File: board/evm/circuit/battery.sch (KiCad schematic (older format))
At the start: 68 parts

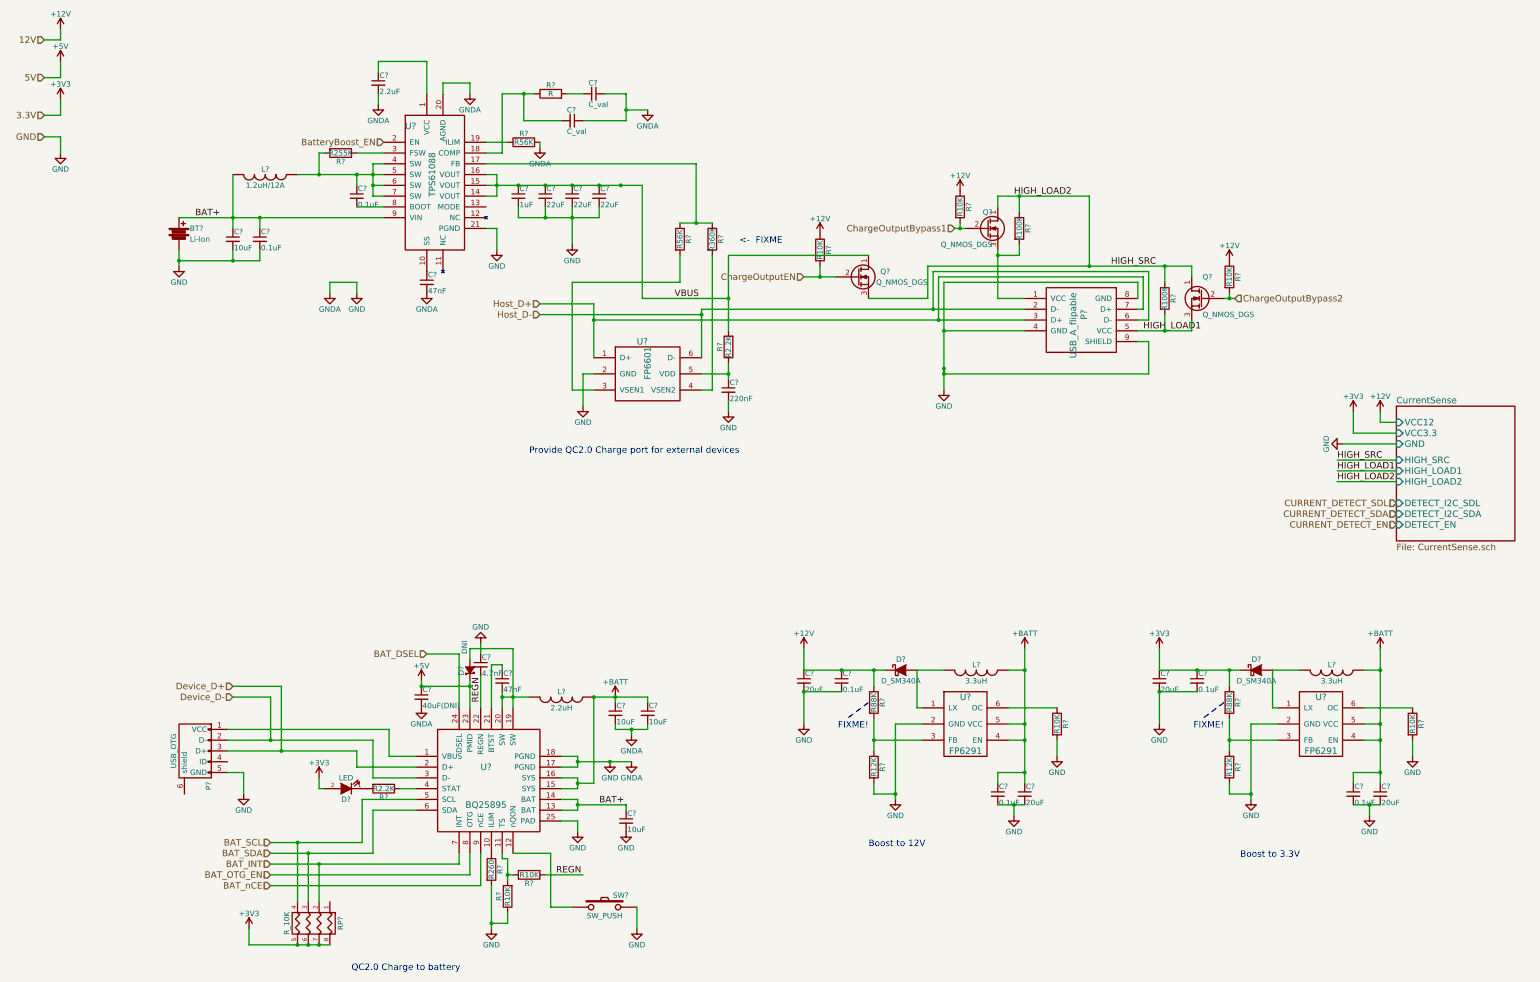
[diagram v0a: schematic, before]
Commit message: minor updates
- add lots of test points
- export usart1
- bug fix
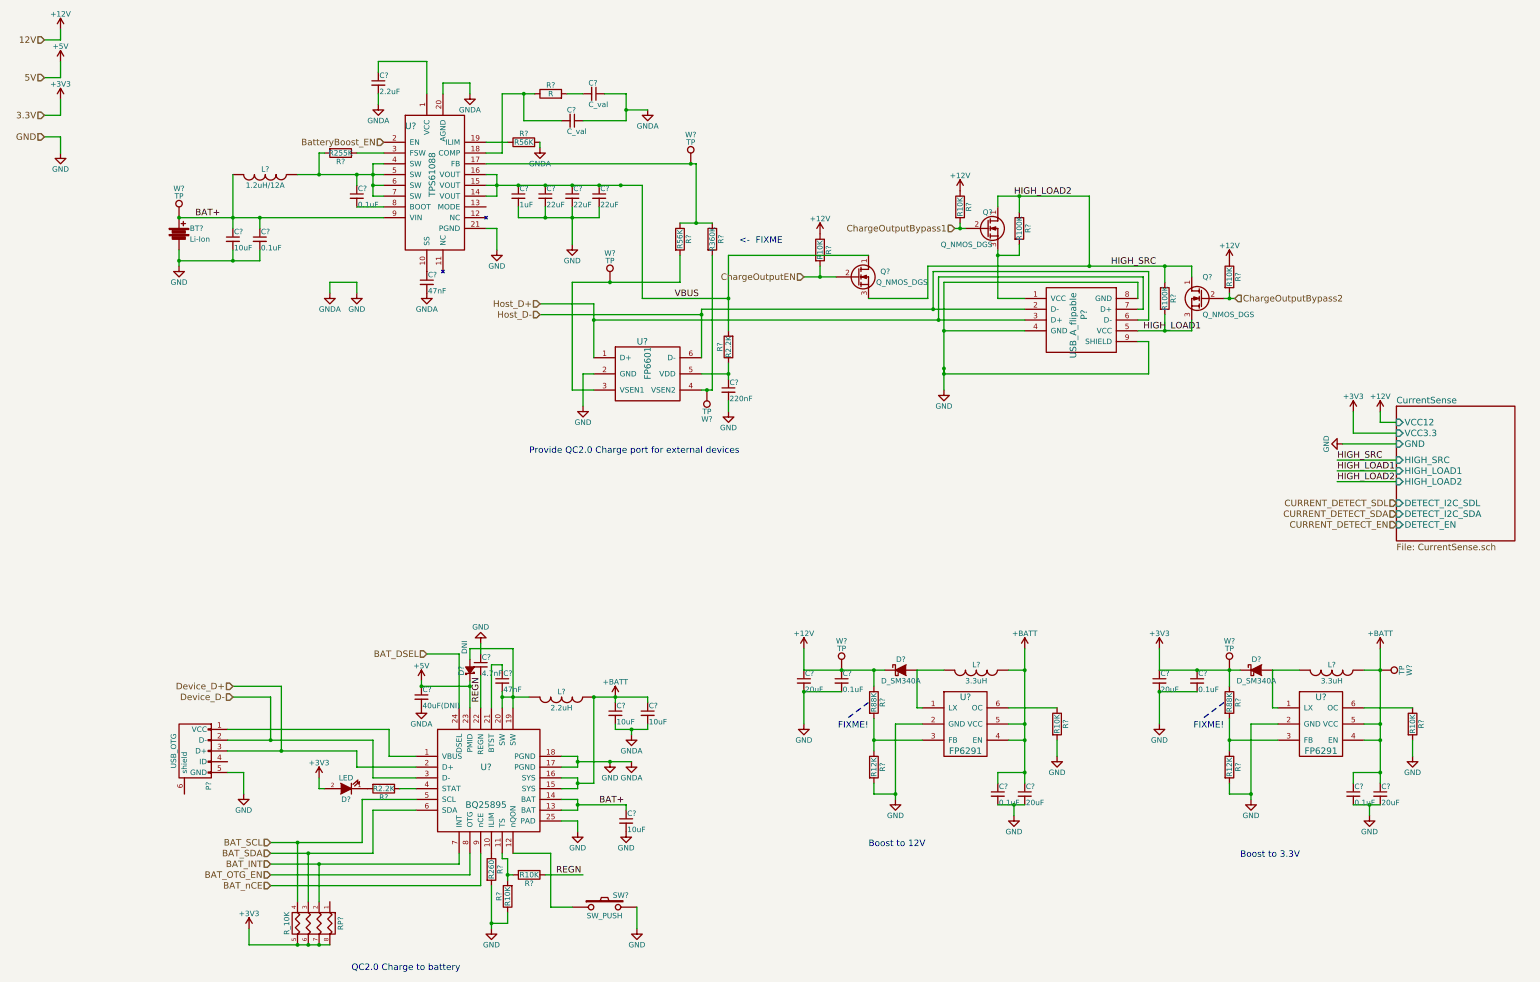
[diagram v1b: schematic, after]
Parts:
- added W? (x7): TP, symbol TEST_1P
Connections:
- net +12V: now also W?.1
- net +3V3: now also W?.1
- net +BATT: now also W?.1
- net BAT+: now also W?.1
- net at R?.1, R?.1, U?.17 (FB): now also W?.1
- net at R?.2, U?.4 (VSEN2): now also W?.1
- net at R?.2, U?.3 (VSEN1): now also W?.1
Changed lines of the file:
@@
 Text HLabel 14000 5200 0    60   Input ~ 0
 CURRENT_DETECT_SDL
+$Comp
+L TEST_1P W?
+U 1 1 57642F75
+P 7450 2050
+F 0 "W?" H 7450 2320 50  0000 C CNN
+F 1 "TP" H 7450 2250 50  0000 C CNN
+F 2 "" H 7650 2050 50  0000 C CNN
+F 3 "" H 7650 2050 50  0000 C CNN
+	1    7450 2050
+	1    0    0    -1
+$EndComp
+Connection ~ 7450 2050
+$Comp
+L TEST_1P W?
+U 1 1 576431FA
+P 6700 3150
+F 0 "W?" H 6700 3420 50  0000 C CNN
+F 1 "TP" H 6700 3350 50  0000 C CNN
+F 2 "" H 6900 3150 50  0000 C CNN
+F 3 "" H 6900 3150 50  0000 C CNN
+	1    6700 3150
+	1    0    0    -1
+$EndComp
+$Comp
+L TEST_1P W?
+U 1 1 57643914
+P 7600 4150
+F 0 "W?" H 7600 4420 50  0000 C CNN
+F 1 "TP" H 7600 4350 50  0000 C CNN
+F 2 "" H 7800 4150 50  0000 C CNN
+F 3 "" H 7800 4150 50  0000 C CNN
+	1    7600 4150
+	-1   0    0    1
+$EndComp
+Connection ~ 7600 4150
+Connection ~ 6700 3150
+$Comp
+L TEST_1P W?
+U 1 1 57647583
+P 13850 6750
+F 0 "W?" H 13850 7020 50  0000 C CNN
+F 1 "TP" H 13850 6950 50  0000 C CNN
+F 2 "" H 14050 6750 50  0000 C CNN
+F 3 "" H 14050 6750 50  0000 C CNN
+	1    13850 6750
+	0    1    1    0
+$EndComp
+$Comp
+L TEST_1P W?
+U 1 1 5764814E
+P 8850 6750
+F 0 "W?" H 8850 7020 50  0000 C CNN
+F 1 "TP" H 8850 6950 50  0000 C CNN
+F 2 "" H 9050 6750 50  0000 C CNN
+F 3 "" H 9050 6750 50  0000 C CNN
+	1    8850 6750
+	1    0    0    -1
+$EndComp
+$Comp
+L TEST_1P W?
+U 1 1 5764877D
+P 12450 6750
+F 0 "W?" H 12450 7020 50  0000 C CNN
+F 1 "TP" H 12450 6950 50  0000 C CNN
+F 2 "" H 12650 6750 50  0000 C CNN
+F 3 "" H 12650 6750 50  0000 C CNN
+	1    12450 6750
+	1    0    0    -1
+$EndComp
+$Comp
+L TEST_1P W?
+U 1 1 5764C228
+P 2700 2550
+F 0 "W?" H 2700 2820 50  0000 C CNN
+F 1 "TP" H 2700 2750 50  0000 C CNN
+F 2 "" H 2900 2550 50  0000 C CNN
+F 3 "" H 2900 2550 50  0000 C CNN
+	1    2700 2550
+	1    0    0    -1
+$EndComp
+Connection ~ 2700 2550
 $EndSCHEMATC

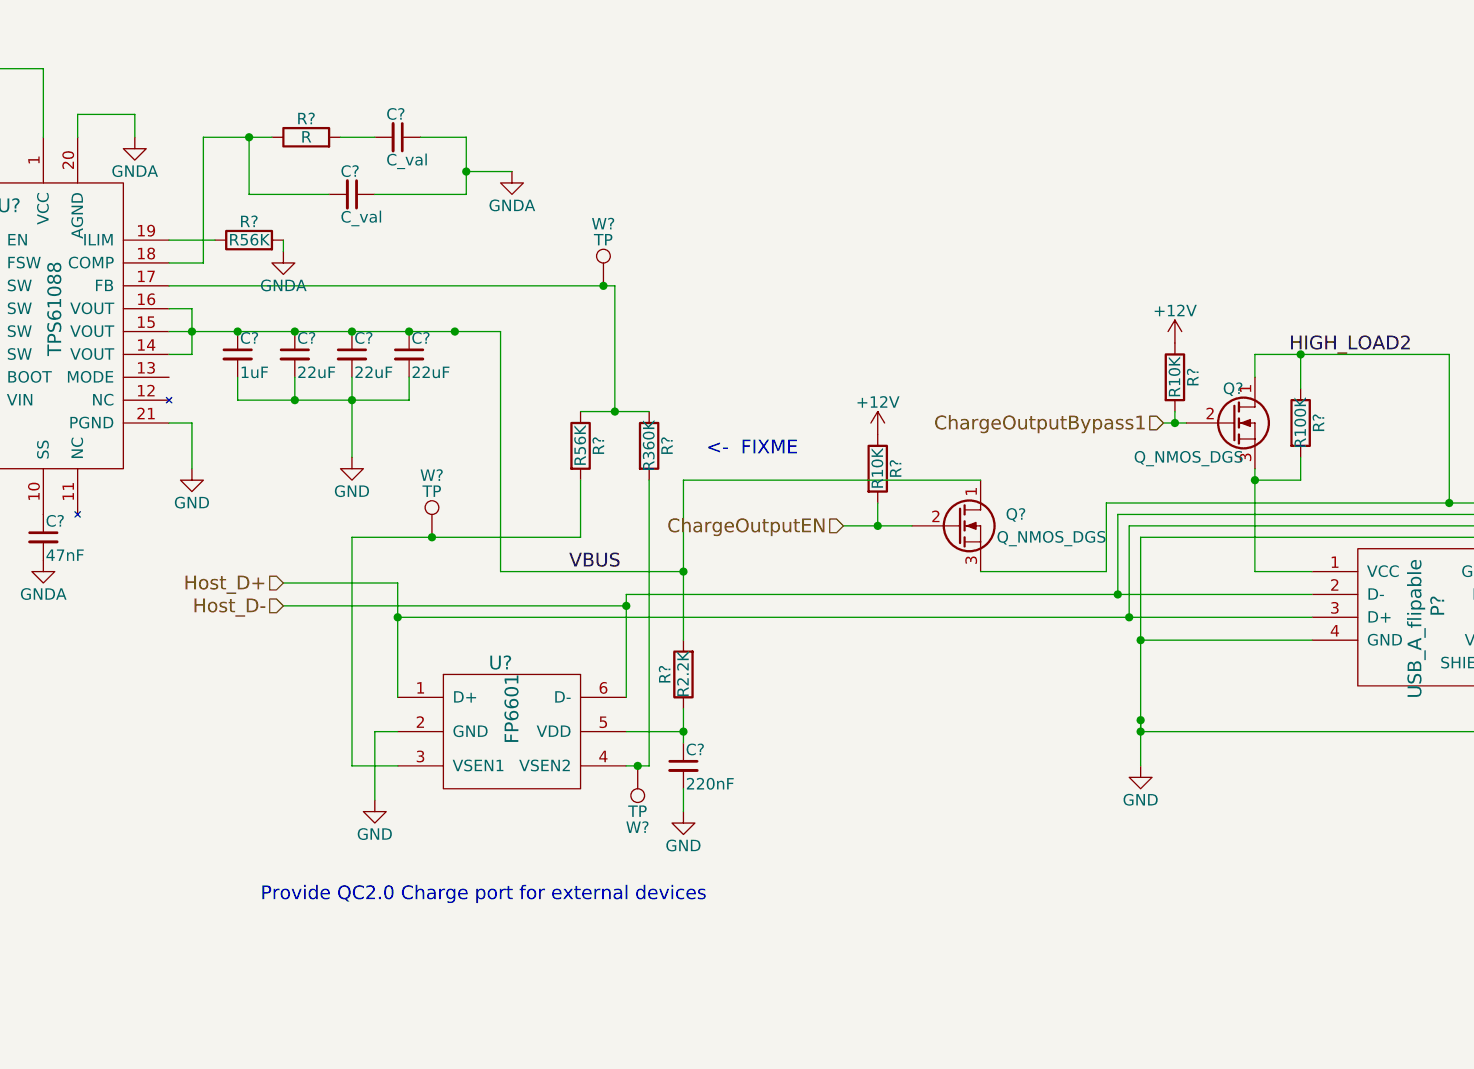
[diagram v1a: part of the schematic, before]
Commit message: upgrade qc2.0 output to qc3.0
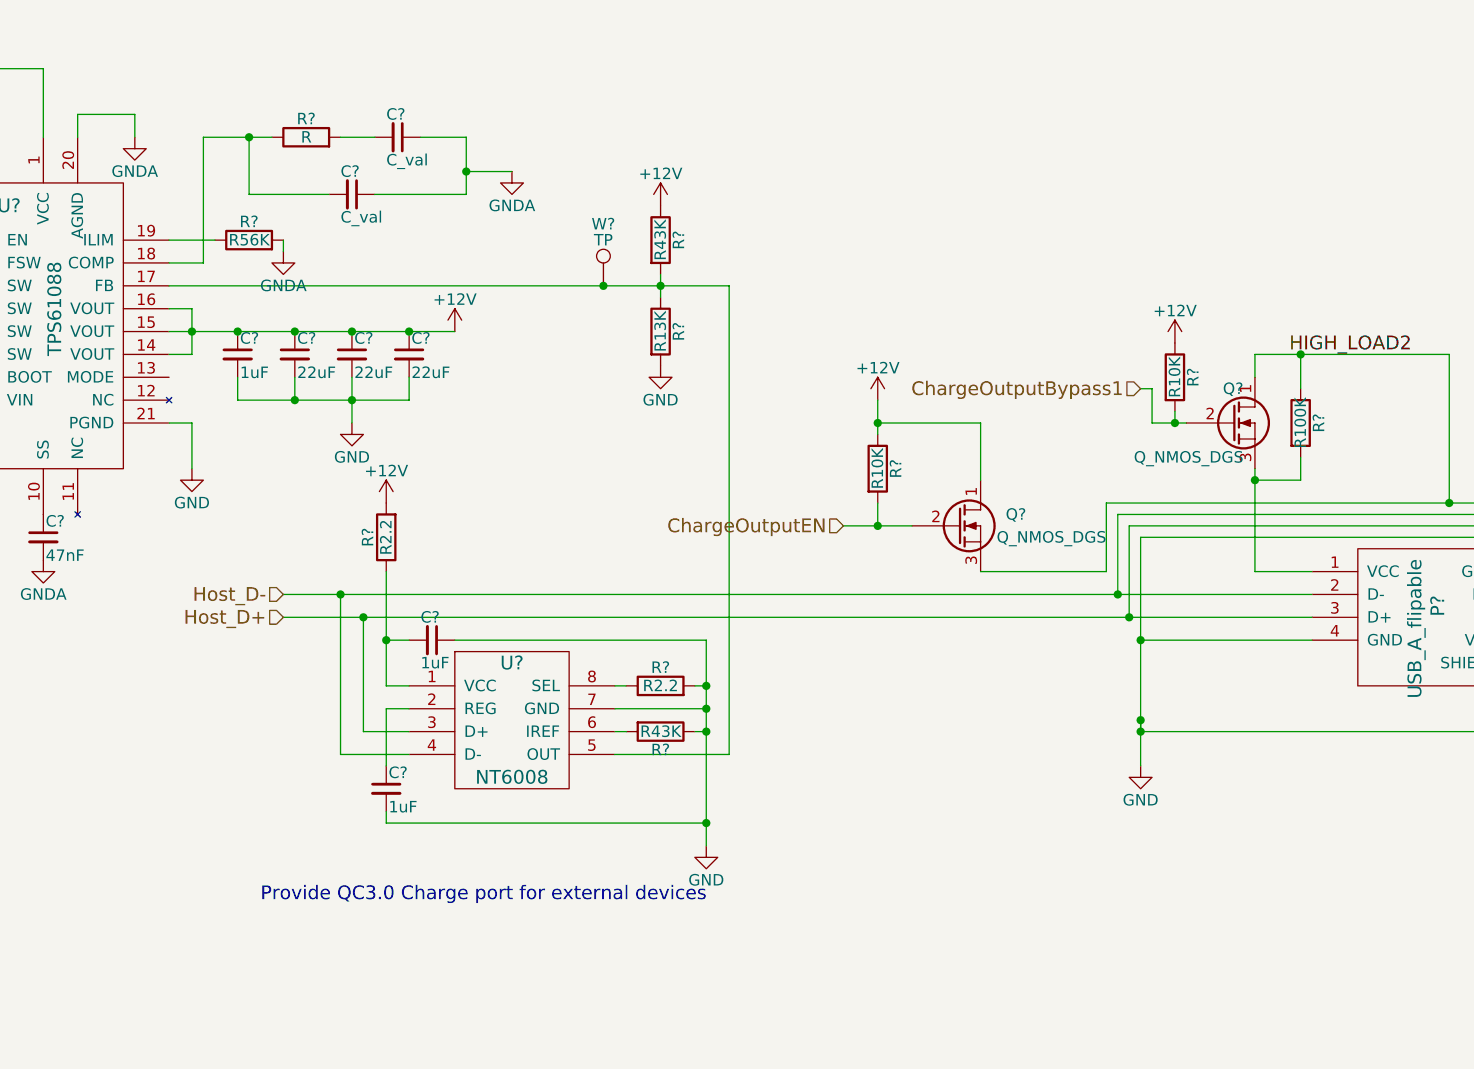
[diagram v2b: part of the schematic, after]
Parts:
- removed C?: 220nF, symbol C_Small
- removed R?: R360K, symbol R
- removed R?: R56K, symbol R
- removed U?: FP6601, symbol FP6601
- removed W? (x2): TP, symbol TEST_1P
- added C? (x2): 1uF, symbol C_Small
- added R?: R2.2, symbol R
- added R? (x2): R43K, symbol R
- added R?: R13K, symbol R
- added U?: NT6008, symbol NT6008
- R?: value R2.2K -> R2.2
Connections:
- net VBUS is gone; now on net +12V: C?.1, C?.1, C?.1, C?.1, Q?.1 (D), R?.2, U?.14 (VOUT), U?.15 (VOUT), U?.16 (VOUT)
- net +12V: now also R?.1
- net GND: now also C?.1, C?.2, R?.1, R?.2, R?.2, U?.7 (GND)
- net Host_D+: now also U?.3 (D+)
- net Host_D-: now also U?.4 (D-)
- net at U?.17 (FB), W?.1: now also R?.1, R?.2, U?.5 (OUT)
- net at R?.1: now also C?.2, U?.1 (VCC)
- new net: C?.1, U?.2 (REG)
- new net: R?.2, U?.6 (IREF)
- new net: R?.1, U?.8 (SEL)
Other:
- note added: "Provide QC3.0 Charge port for external devices"
- note removed: "<- FIXME"
- note removed: "Provide QC2.0 Charge port for external devices"
- moved on the sheet: R?

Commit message: working on drc
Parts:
- gave numbers to parts that had none: 76

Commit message: working on footprint
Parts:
- BT1: footprint (none) -> Connect:PINHEAD1-2
- C38, C42, C47, C49, C52, C54, C55, C56, C57, C60, C61, C64: footprint (none) -> Capacitors_SMD:C_0805
- C39, C40, C43, C44, C45, C48, C51, C58, C59, C62, C63: footprint (none) -> Capacitors_SMD:C_0402
- C41, C46, C50, C53: footprint (none) -> Capacitors_SMD:C_0603
- D11: footprint (none) -> LEDs:LED_0805
- D12: value DNI -> SS14(DNI); footprint (none) -> Diodes_SMD:SMA_Standard
- D13, D14: value D_SM340A -> D_SS14; footprint (none) -> Diodes_SMD:SMA_Standard
- R16, R17, R18, R19, R20, R21, R22, R23, R24, R25, R26, R27, R28, R29, R30, R31, R32, R33, R34, R35, R36, R37, R38, RP8: footprint (none) -> Resistors_SMD:R_0402
- SW9: footprint (none) -> Buttons_Switches_SMD:SW_SPST_B3U-1000P
- W49, W50, W51, W52, W53: footprint (none) -> Connect:PINTST

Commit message: still working on footprint
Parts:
- U12: footprint (none) -> My custom footprint:S-PVQFN-N20
- U14: footprint (none) -> My custom footprint:TSOT23-8L
- U15, U16: footprint (none) -> TO_SOT_Packages_SMD:SOT-23-6
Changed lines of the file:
@@
 LIBS:contrib
 LIBS:valves
+LIBS:stm8
+LIBS:stm32
+LIBS:74xgxx
+LIBS:ac-dc
+LIBS:actel
 LIBS:Altera
+LIBS:analog_devices
+LIBS:battery_management
+LIBS:bbd
+LIBS:brooktre
+LIBS:cmos_ieee
+LIBS:dc-dc
+LIBS:diode
+LIBS:elec-unifil
+LIBS:ESD_Protection
+LIBS:ftdi
+LIBS:gennum
+LIBS:graphic
+LIBS:hc11
+LIBS:ir
+LIBS:Lattice
+LIBS:logo
+LIBS:maxim
+LIBS:microchip_dspic33dsc
+LIBS:microchip_pic10mcu
+LIBS:microchip_pic12mcu
+LIBS:microchip_pic16mcu
+LIBS:microchip_pic18mcu
+LIBS:microchip_pic32mcu
+LIBS:motor_drivers
+LIBS:msp430
+LIBS:nordicsemi
+LIBS:nxp_armmcu
+LIBS:onsemi
+LIBS:Oscillators
+LIBS:powerint
+LIBS:Power_Management
+LIBS:pspice
+LIBS:references
+LIBS:relays
+LIBS:rfcom
+LIBS:sensors
+LIBS:silabs
+LIBS:supertex
+LIBS:switches
+LIBS:transf
+LIBS:ttl_ieee
+LIBS:video
+LIBS:Worldsemi
+LIBS:Xicor
+LIBS:Zilog
 LIBS:my_kicad
-LIBS:Oscillators
 LIBS:oh-my-keyboard-cache
 EELAYER 25 0
@@
 F 0 "U12" H 4850 2800 60  0000 C CNN
 F 1 "TPS61088" V 5050 2350 60  0000 C CNN
-F 2 "" H 5200 2250 60  0001 C CNN
+F 2 "My custom footprint:S-PVQFN-N20" H 5200 2250 60  0001 C CNN
 F 3 "" H 5200 2250 60  0000 C CNN
 	1    5200 2250
@@
 F 0 "U15" H 10000 7500 60  0000 C CNN
 F 1 "FP6291" H 10000 7000 60  0000 C CNN
-F 2 "" H 9950 7200 60  0001 C CNN
+F 2 "TO_SOT_Packages_SMD:SOT-23-6" H 9950 7200 60  0001 C CNN
 F 3 "" H 9950 7200 60  0000 C CNN
 	1    10000 7250
@@
 F 0 "U16" H 13300 7500 60  0000 C CNN
 F 1 "FP6291" H 13300 7000 60  0000 C CNN
-F 2 "" H 13250 7200 60  0001 C CNN
+F 2 "TO_SOT_Packages_SMD:SOT-23-6" H 13250 7200 60  0001 C CNN
 F 3 "" H 13250 7200 60  0000 C CNN
 	1    13300 7250
@@
 F 0 "U14" H 7050 4200 60  0000 C CNN
 F 1 "NT6008" H 7050 3700 60  0000 C CNN
-F 2 "" H 7300 3500 60  0001 C CNN
+F 2 "My custom footprint:TSOT23-8L" H 7300 3500 60  0001 C CNN
 F 3 "" H 7300 3500 60  0000 C CNN
 	1    7050 3950
